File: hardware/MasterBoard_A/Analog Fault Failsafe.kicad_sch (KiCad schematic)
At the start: 0 parts

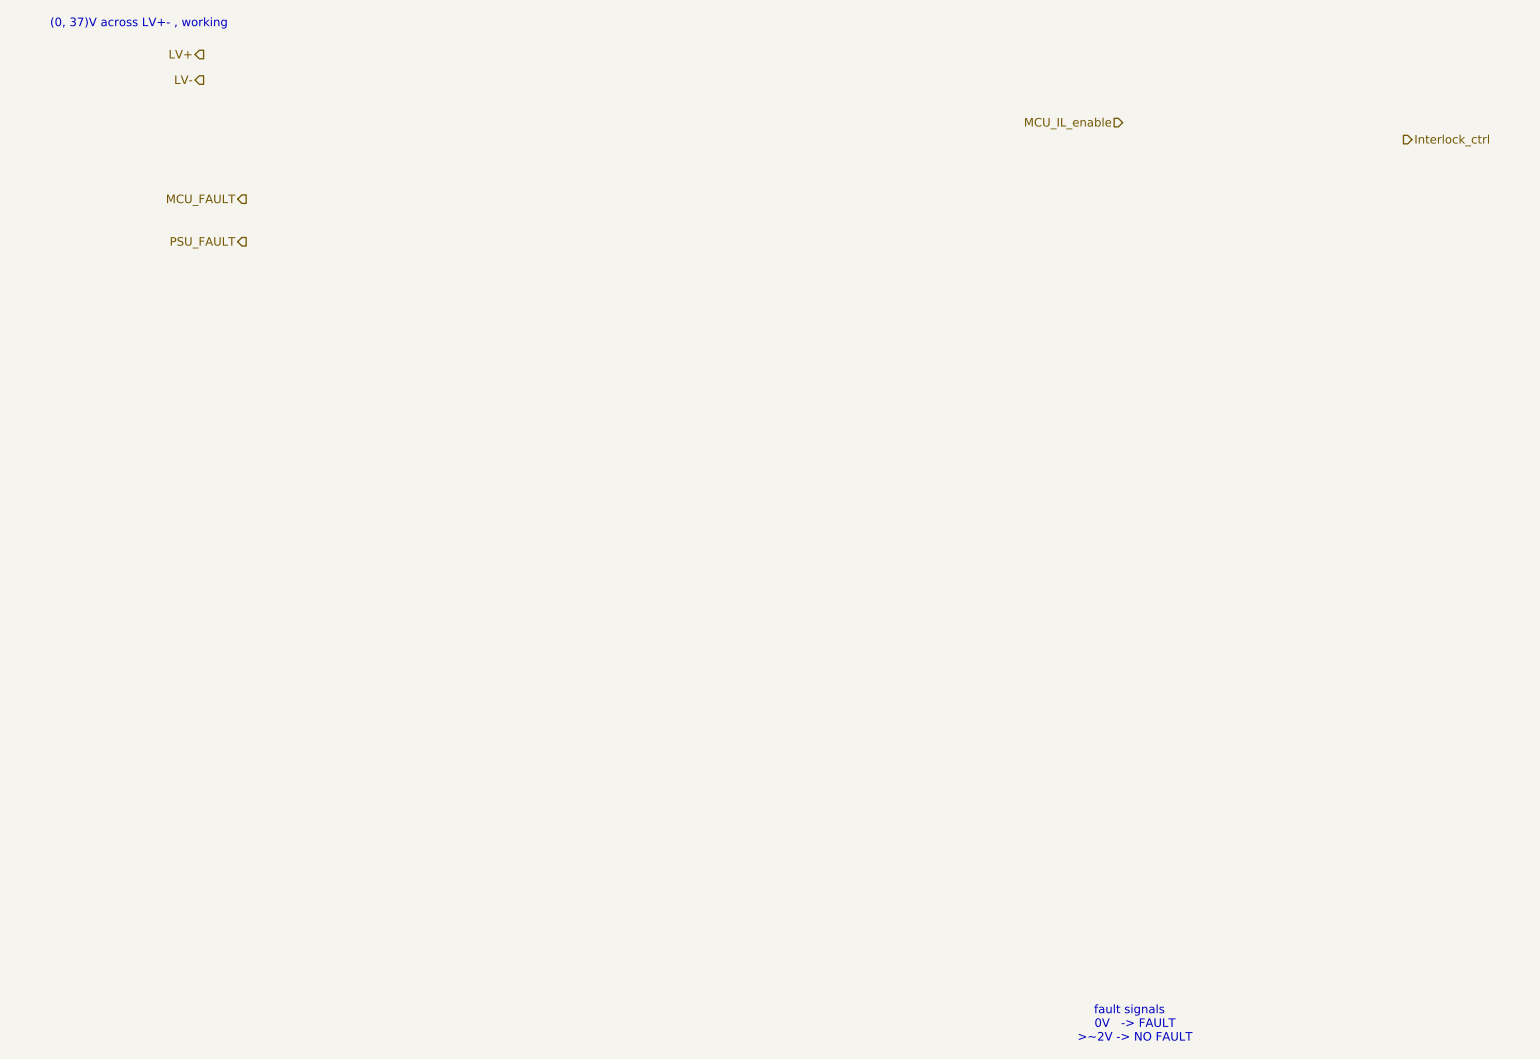
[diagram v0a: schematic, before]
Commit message: near final
missing direct MCU connections, pin map excel sheet needs piddled with. schematic needs reviewed
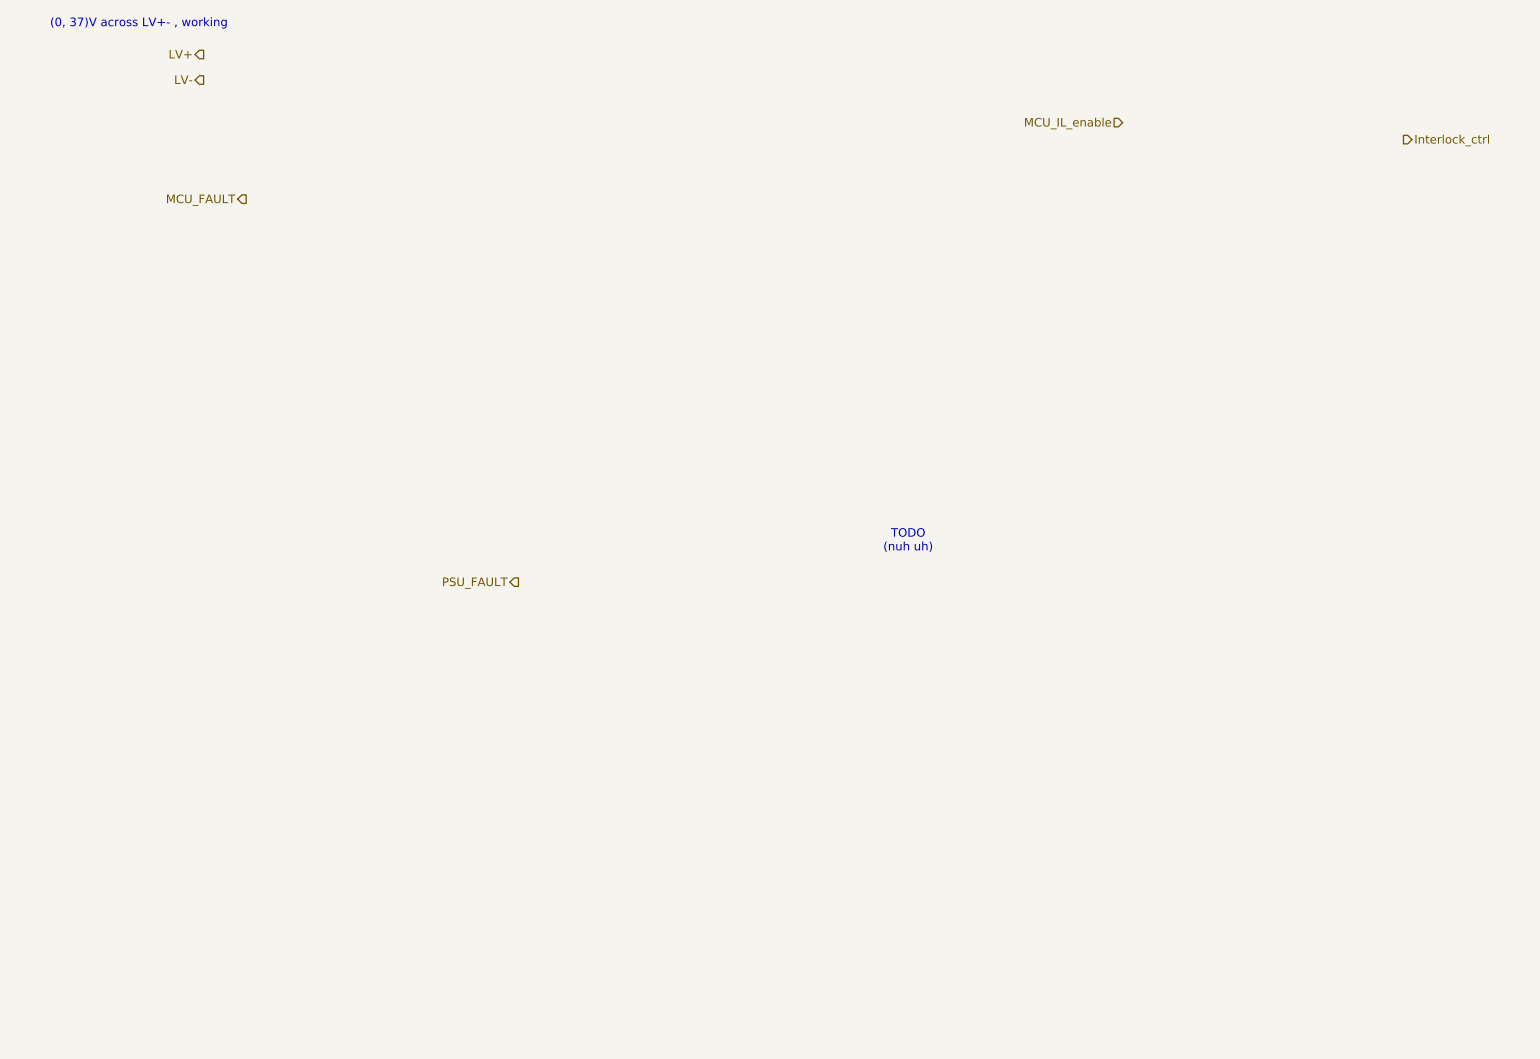
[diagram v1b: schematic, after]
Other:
- note added: "TODO (nuh uh)"
- note removed: "fault signals 0V -> FAULT >~2V -> NO FAULT"
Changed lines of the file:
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@@
 	(generator_version "9.0")
 	(paper "A4")
-	(text "fault signals \n   0V   -> FAULT\n   >~2V -> NO FAULT"
+	(text "TODO\n(nuh uh)"
 		(exclude_from_sim no)
-		(at 183.896 170.18 0)
+		(at 150.876 98.044 0)
 		(effects
 			(font
-				(face "Impact")
 				(size 1.27 1.27)
 			)
@@
 	(hierarchical_label "PSU_FAULT"
 		(shape output)
-		(at 52.07 53.34 180)
+		(at 92.71 104.14 180)
 		(effects
 			(font

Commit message: mb v1.1 on da way
shuffled around stuff. review notes. made notes. glory to those who look forward and all that fuzz
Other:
- company: (none) -> UTA Racing
- title: (none) -> BeeMS Master Board (A)
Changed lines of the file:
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@@
 	(generator_version "9.0")
 	(paper "A4")
+	(title_block
+		(title "BeeMS Master Board (A)")
+		(company "UTA Racing")
+		(comment 1 "Files at github.com/Gregification/BeeMS")
+	)
 	(text "TODO\n(nuh uh)"
 		(exclude_from_sim no)
